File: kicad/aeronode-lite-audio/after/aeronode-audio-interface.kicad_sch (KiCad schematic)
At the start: 22 parts, among them J1 Conn_01x06_Pin, J10 AIRCRAFT PANEL, J11 HEADSET, J2 Conn_01x08_Pin, J3 Conn_01x10_Pin, J4 Conn_01x06_Pin, K1 G6K-2F-Y, K2 G6K-2F-Y, Q1 2N7002, Q2 2N7002, T1 SM-LP-5001

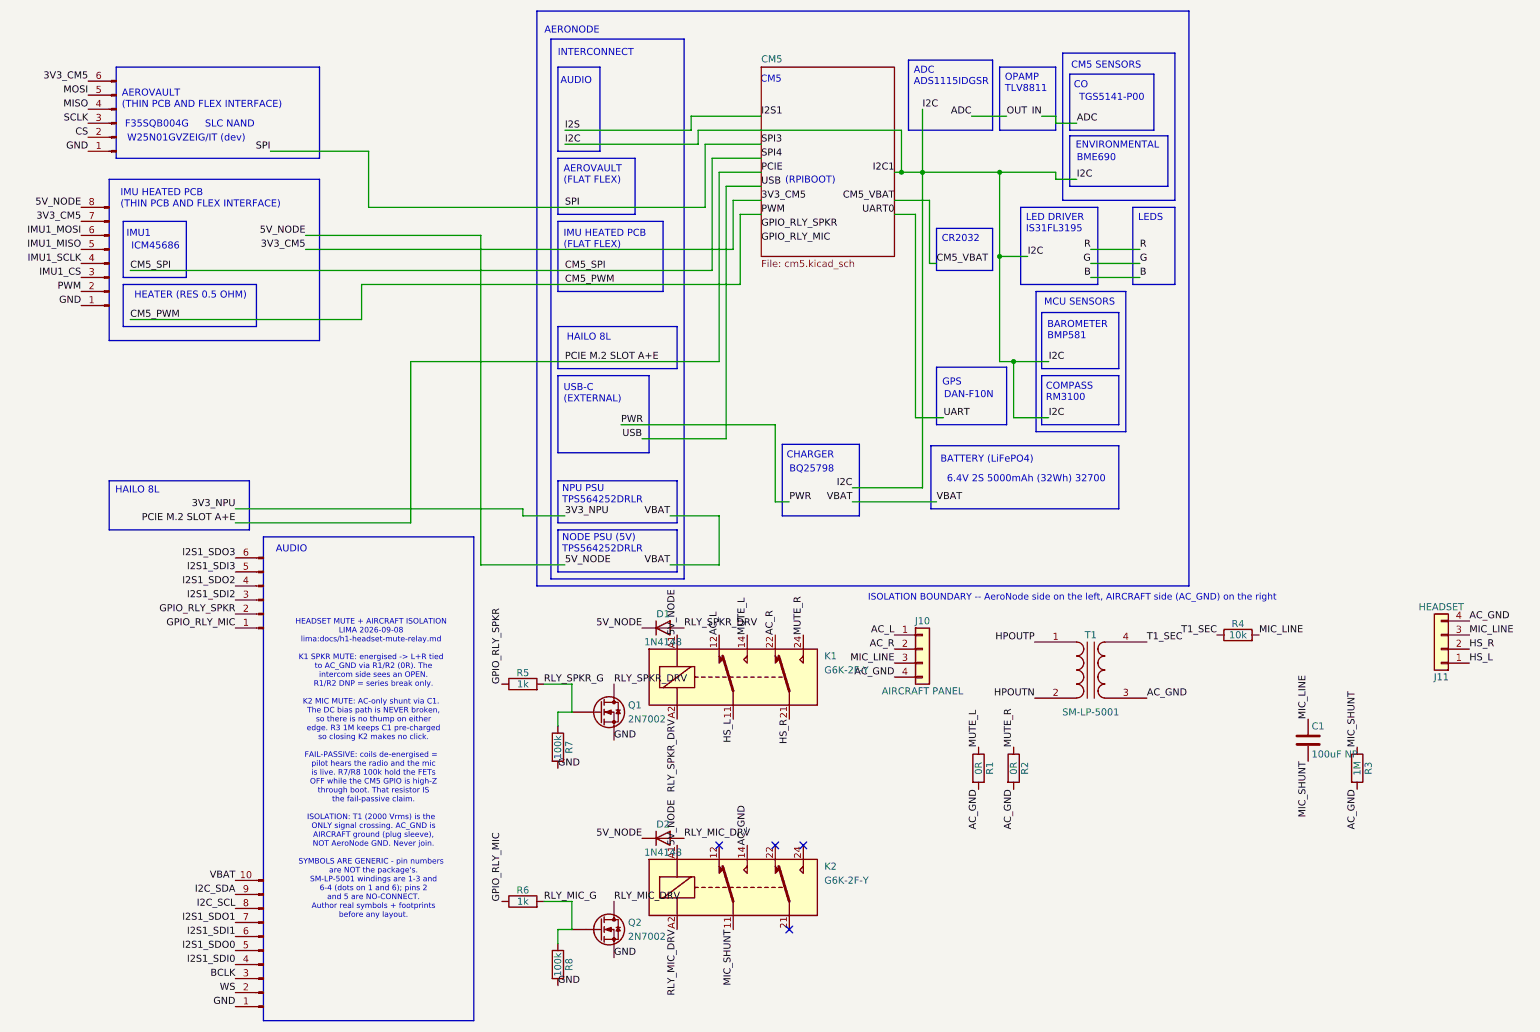
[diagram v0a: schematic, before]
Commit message: [LIMA] audio mute: moved to its own hierarchical sheet, and an instrument caught lying
Peter asked for it on its own schematic so nothing overlays. AUDIO MUTE +
ISOLATION is now audio-mute.kicad_sch (page 3), matching the cm5.kicad_sch
pattern already in the project.

- Restored the parent to its original bytes first (md5 verified against the
  pre-edit backup) rather than unpicking ~45 labels by hand, then added only
  the sheet symbol and its six pins.
- Six sheet pins via KiCAD's own Import Sheet Pins; validate_sheet_pins clean.
  Aircraft-side nets now stay local to the sub-sheet instead of leaking into
  the parent namespace - a second reason the sub-sheet is the right home.
- No overlays. The change that did it: rotate K1/K2 90 degrees so the contacts
  face left/right at 2.54mm pitch and labels stack like connector pin names.
- ERC 41 = untouched baseline. Netlist verified on both sides of the boundary.

SCAR: Konnect's validate_wire_connections reported "0 floating endpoints,
valid: true" while KiCAD's ERC reported two wires connected to nothing - and
the netlist proved ERC right: Q1.G, R5.2 and R7.1 were on no net at all. The
wires rendered convincingly and passed the friendly check. Junction dots did
not fix it; a net label on the gate node did. validate_wire_connections is not
ERC, and a render that looks connected is not a connected schematic.

Co-Authored-By: Claude Opus 5 <noreply@anthropic.com>
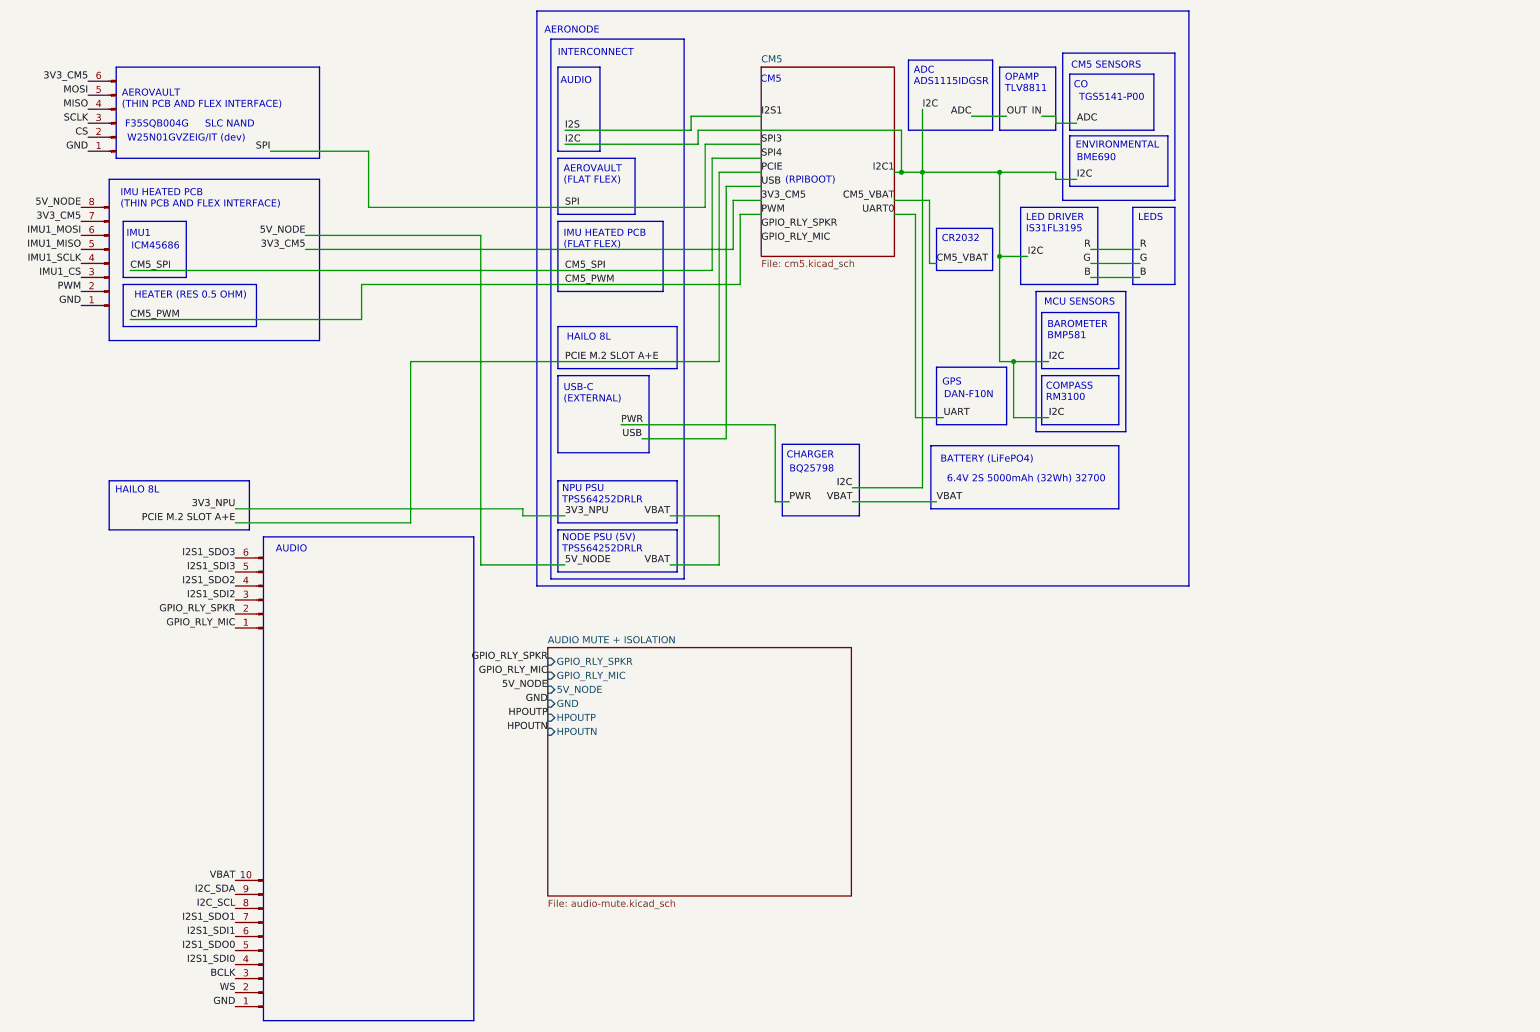
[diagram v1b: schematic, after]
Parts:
- removed C1: 100uF NP, symbol Device:C
- removed D1, D2: 1N4148, symbol Device:D
- removed J10: AIRCRAFT PANEL, symbol Connector_Generic:Conn_01x04
- removed J11: HEADSET, symbol Connector_Generic:Conn_01x04
- removed K1, K2: G6K-2F-Y, symbol Relay:Relay_DPDT
- removed Q1, Q2: 2N7002, symbol Device:Q_NMOS
- removed R1, R2: 0R, symbol Device:R
- removed R3: 1M, symbol Device:R
- removed R4: 10k, symbol Device:R
- removed R5, R6: 1k, symbol Device:R
- removed R7, R8: 100k, symbol Device:R
- removed T1: SM-LP-5001, symbol Device:Transformer_1P_1S
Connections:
- no-connect marks 4 -> 0
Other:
- added sheet AUDIO MUTE + ISOLATION (audio-mute.kicad_sch)
- note removed: "HEADSET MUTE + AIRCRAFT ISOLATION LIMA 2026-09-08 lima:docs/h1-headset-mute-relay.md K1 SPKR MUTE: energised -> L+R tied to AC_GND via R1/R2 (0R). The intercom side sees an OPEN. R1/R2 DNP = series break only. K2 MIC MUTE: AC-only shunt via C1. The DC bias path is NEVER broken, so there is no thump on either edge. R3 1M keeps C1 pre-charged so closing K2 makes no click. FAIL-PASSIVE: coils de-ene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"
- note removed: "ISOLATION BOUNDARY -- AeroNode side on the left, AIRCRAFT side (AC_GND) on the right"

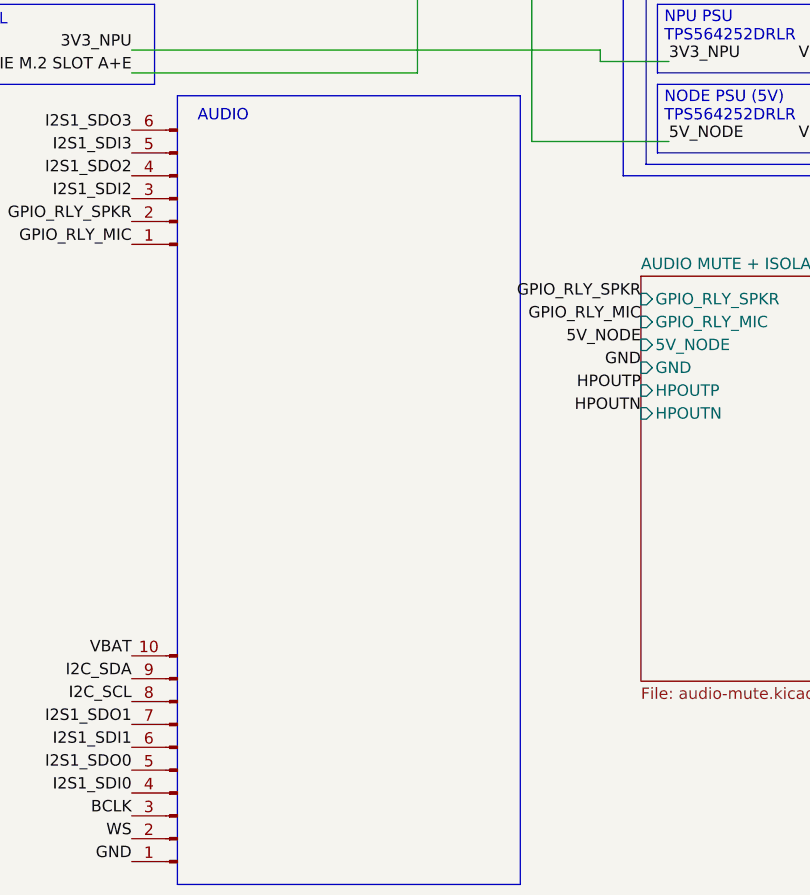
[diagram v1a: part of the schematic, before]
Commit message: [LIMA] analog-mics: three mics on ADC0/1/2 - and a spec band I misread as physics
Peter asked for boom-voice + ANC feedforward + ANC feedback. New hierarchical
sheet analog-mics.kicad_sch (page 4). Per channel: 100R + 1uF supply filter and
1uF coupling on BOTH legs (OUT and the module's local GND), pseudo-differential,
mirroring the EVB's Figure 8 topology.

- Channel budget is now FULL: the ADAU1860 has exactly three ADCs, zero spare.
- These are AeroNode's own mics on our rail and our GND, so they never touch
  AC_GND and section 11.3's "T1 is the only crossing" still stands literally.
  No transformers needed here - had they been taps off the headset, each would
  have needed one.
- ERC 42, not the usual 41. The extra is "Label not connected: 3V3_MIC", which
  is ERC correctly reporting that the mic rail has no source. Tying it to
  3V3_CM5 to make the number pretty would be the wrong trade, since ANC noise
  performance is set by the mic supply.
- validate_sheet_pins clean across 14 pins; /GND now spans all three sheets.

CORRECTION TO MYSELF, caught before commit: I wrote that T1's 200 Hz-4 kHz spec
band would cut ANC off below 200 Hz. Wrong. That band is Bourns' 600R telecom
condition. In this circuit - 160R of paralleled earphones from a low-Z drive -
the Thevenin R across the 3.8 H magnetising inductance is 81.6R, giving a 3.4 Hz
corner and -0.020 dB at 50 Hz. Flat across the ANC band. A vendor's specified
band is the condition they guaranteed, not the physics of your circuit.

Left open, not decided: ANC's real blocker is that K1 is a changeover, so the
DAC only reaches the earcup while K1 is energised, where anti-noise must be
permanently connected. And whether the target headset already has its own ANR.

Co-Authored-By: Claude Opus 5 <noreply@anthropic.com>
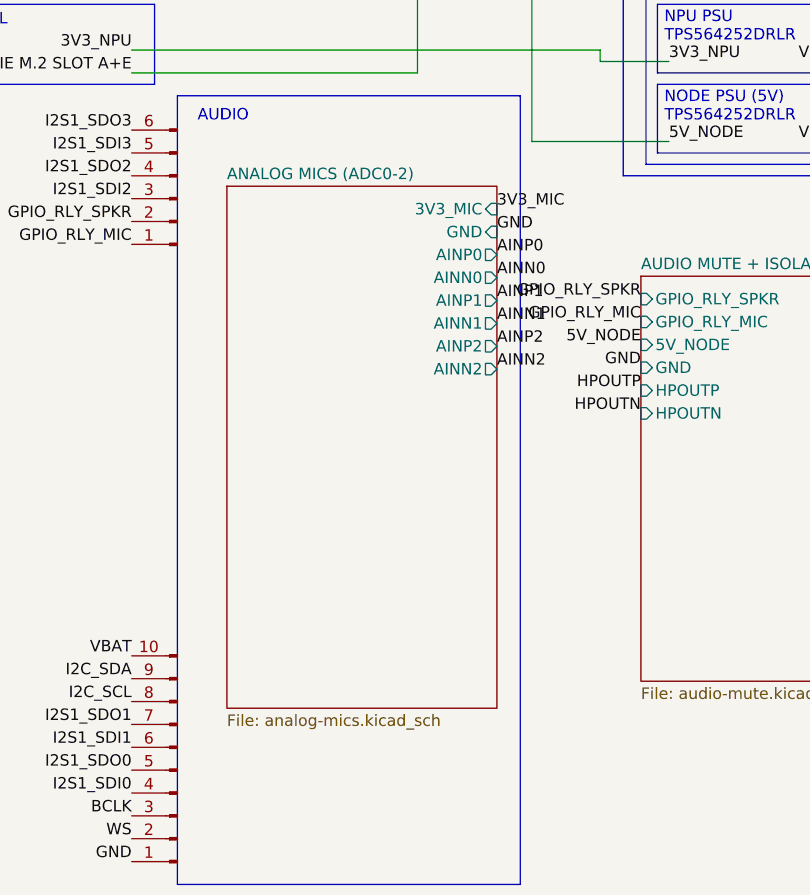
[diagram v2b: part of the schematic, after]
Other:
- added sheet ANALOG MICS (ADC0-2) (analog-mics.kicad_sch)
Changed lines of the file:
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@@
+		)
+	)
+	(label "GND"
+		(at 99 123.08 0)
+		(effects
+			(font
+				(size 1.27 1.27)
+			)
+			(justify left bottom)
+		)
+	)
+	(label "3V3_MIC"
+		(at 99 120.54 0)
+		(effects
+			(font
+				(size 1.27 1.27)
+			)
+			(justify left bottom)
+		)
+	)
+	(label "AINP0"
+		(at 99 125.62 0)
+		(effects
+			(font
+				(size 1.27 1.27)
+			)
+			(justify left bottom)
+		)
+	)
+	(label "AINN0"
+		(at 99 128.16 0)
+		(effects
+			(font
+				(size 1.27 1.27)
+			)
+			(justify left bottom)
+		)
+	)
+	(label "AINP1"
+		(at 99 130.7 0)
+		(effects
+			(font
+				(size 1.27 1.27)
+			)
+			(justify left bottom)
+		)
+	)
+	(label "AINN1"
+		(at 99 133.24 0)
+		(effects
+			(font
+				(size 1.27 1.27)
+			)
+			(justify left bottom)
+		)
+	)
+	(label "AINP2"
+		(at 99 135.78 0)
+		(effects
+			(font
+				(size 1.27 1.27)
+			)
+			(justify left bottom)
+		)
+	)
+	(label "AINN2"
+		(at 99 138.32 0)
+		(effects
+			(font
+				(size 1.27 1.27)
+			)
+			(justify left bottom)
 		)
 	)
@@
 				)
 			)
+		)
+	)
+	(sheet
+		(at 69 118)
+		(size 30 58)
+		(fields_autoplaced)
+		(stroke
+			(width 0.1524)
+			(type solid)
+		)
+		(fill
+			(color 0 0 0 0.0)
+		)
+		(property "Sheetname" "ANALOG MICS (ADC0-2)"
+			(at 69 117.365 0)
+			(effects
+				(font
+					(size 1.27 1.27)
+				)
+				(justify left bottom)
+			)
+		)
+		(property "Sheetfile" "analog-mics.kicad_sch"
+			(at 69 176.635 0)
+			(effects
+				(font
+					(size 1.27 1.27)
+				)
+				(justify left top)
+			)
+		)
+		(pin "3V3_MIC" input
+			(at 99 120.54 0)
+		)
+		(pin "GND" input
+			(at 99 123.08 0)
+		)
+		(pin "AINP0" output
+			(at 99 125.62 0)
+		)
+		(pin "AINN0" output
+			(at 99 128.16 0)
+		)
+		(pin "AINP1" output
+			(at 99 130.7 0)
+		)
+		(pin "AINN1" output
+			(at 99 133.24 0)
+		)
+		(pin "AINP2" output
+			(at 99 135.78 0)
+		)
+		(pin "AINN2" output
+			(at 99 138.32 0)
+		)
+		(instances
+			(project "aeronode-audio-interface"
+				(path "/0cbb3bbb-8297-40d4-b3a9-e92b3d8d375c"
+					(page "4")
+				)
+			)
